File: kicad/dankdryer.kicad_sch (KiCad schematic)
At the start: 25 parts, among them J11 testpin, J13 barreljack, J8 motor, J9 Conn_01x04, SW2 bootmode, U1 TPS62132, U6 ESP32-C6-MINI-1U

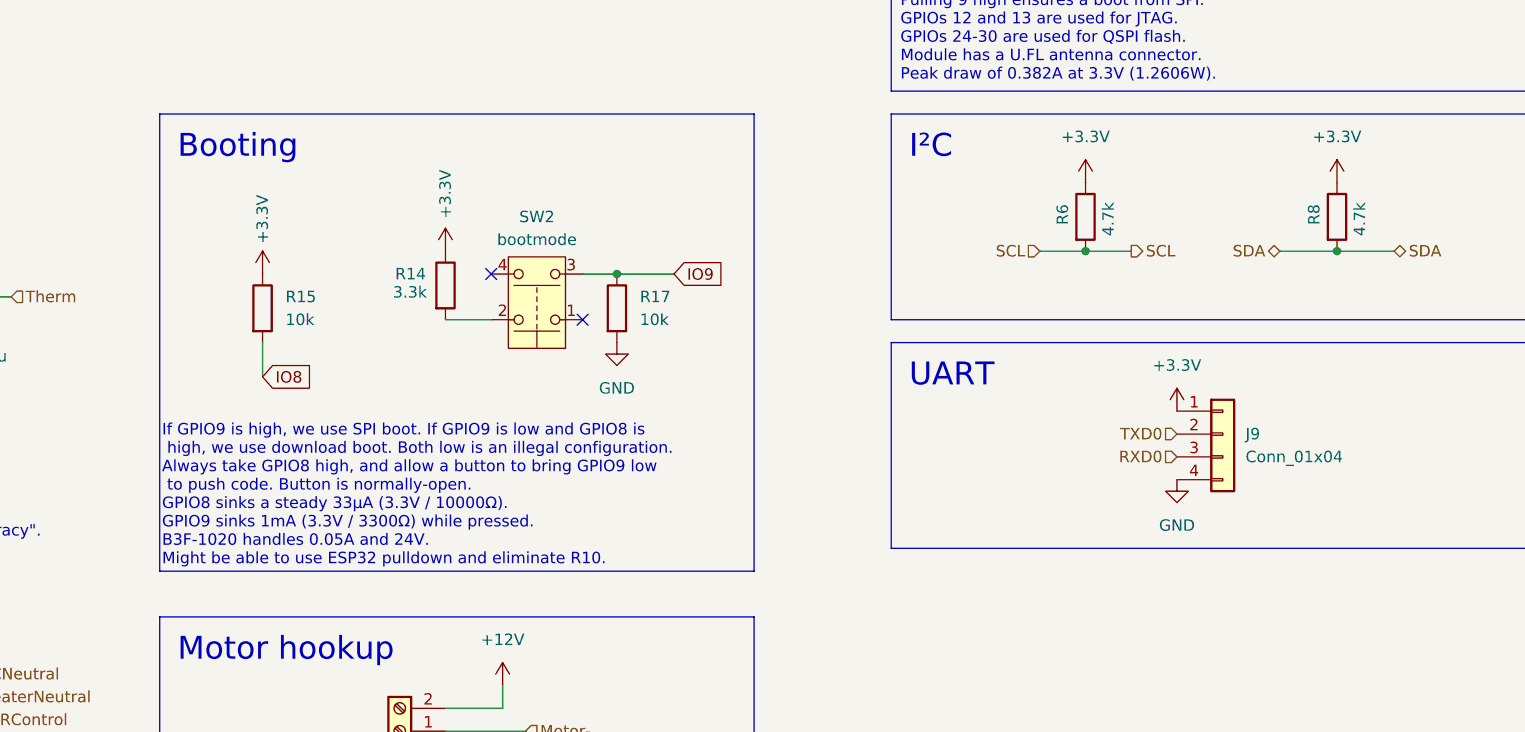
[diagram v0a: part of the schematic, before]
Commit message: invert logic for gpio9, erp
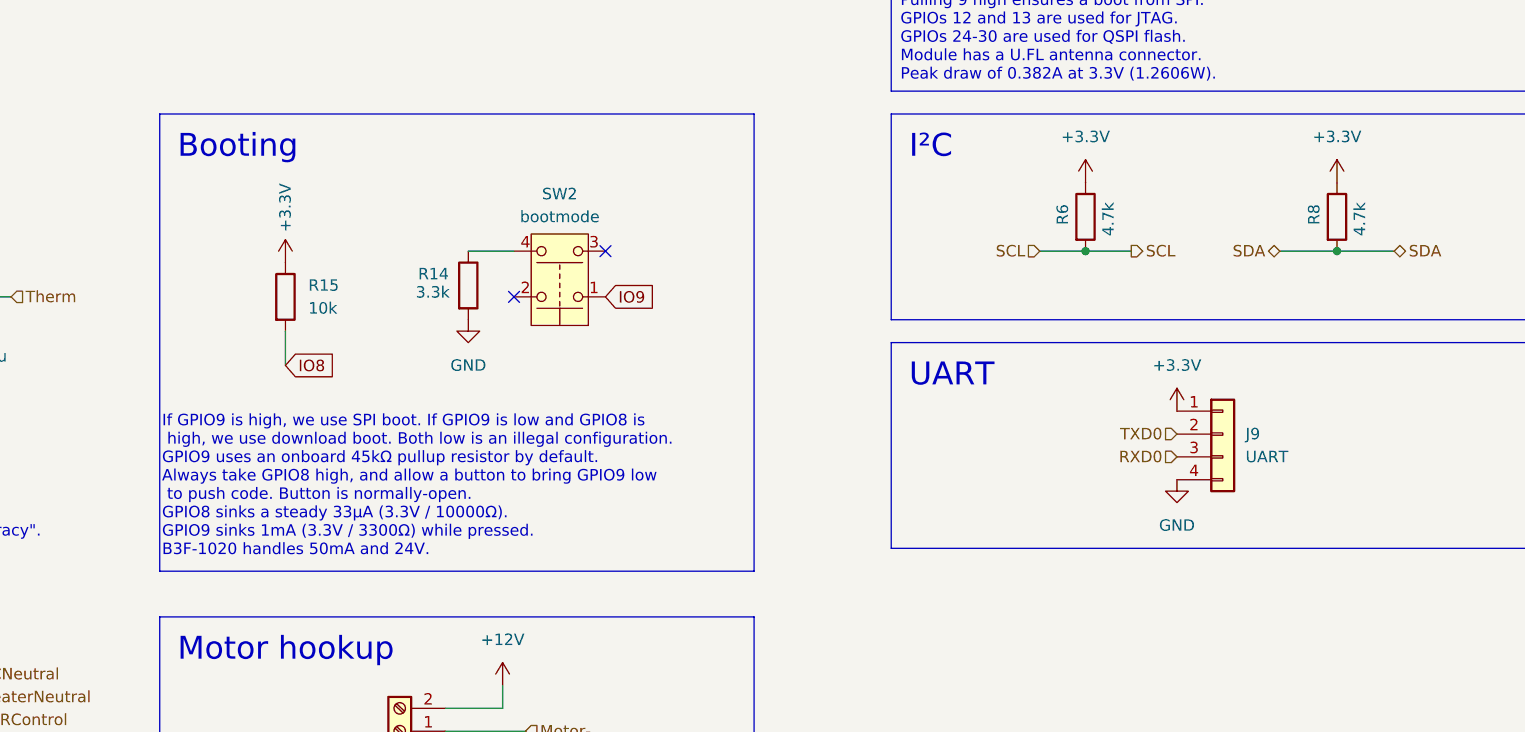
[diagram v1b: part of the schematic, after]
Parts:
- removed R17: 10k, Resistor_SMD:R_1206_3216Metric_Pad1.30x1.75mm_HandSolder, symbol Device:R
- J9: value Conn_01x04 -> UART
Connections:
- net +3.3V: no longer R14.1
- net GND: now also R14.2
- net IO9: now also SW2.1; no longer SW2.3
- net at SW2.2: no longer R14.2
- net at SW2.4: now also R14.1
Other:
- note added: "If GPIO9 is high, we use SPI boot. If GPIO9 is low and GPIO8 is high, we use download boot. Both low is an illegal configuration. GPIO9 uses an onboard 45kΩ pullup resistor by default. Always take GPIO8 high, and allow a button to bring GPIO9 low to push code. Button is normally-open. GPIO8 sinks a steady 33μA (3.3V / 10000Ω). GPIO9 sinks 1mA (3.3V / 3300Ω) while pressed. B3F-1020 handles 50mA an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"
- note removed: "If GPIO9 is high, we use SPI boot. If GPIO9 is low and GPIO8 is high, we use download boot. Both low is an illegal configuration. Always take GPIO8 high, and allow a button to bring GPIO9 low to push code. Button is normally-open. GPIO8 sinks a steady 33μA (3.3V / 10000Ω). GPIO9 sinks 1mA (3.3V / 3300Ω) while pressed. B3F-1020 handles 0.05A and 24V. Might be able to use ESP32 pulldown and elimina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"
- moved on the sheet: R14, R15, SW2

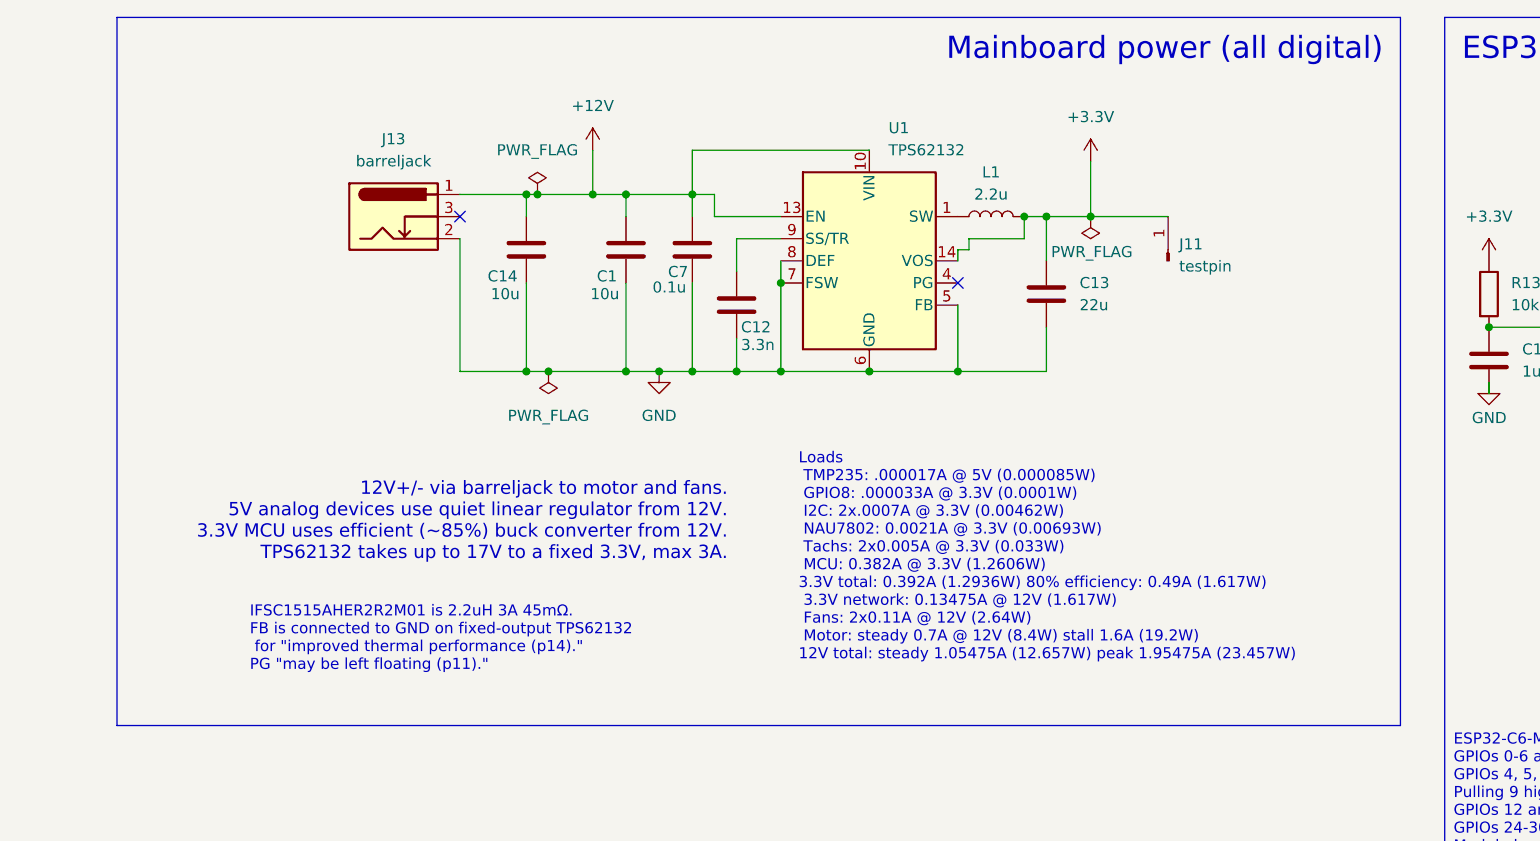
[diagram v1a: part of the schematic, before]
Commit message: switch from AKL_R to regular
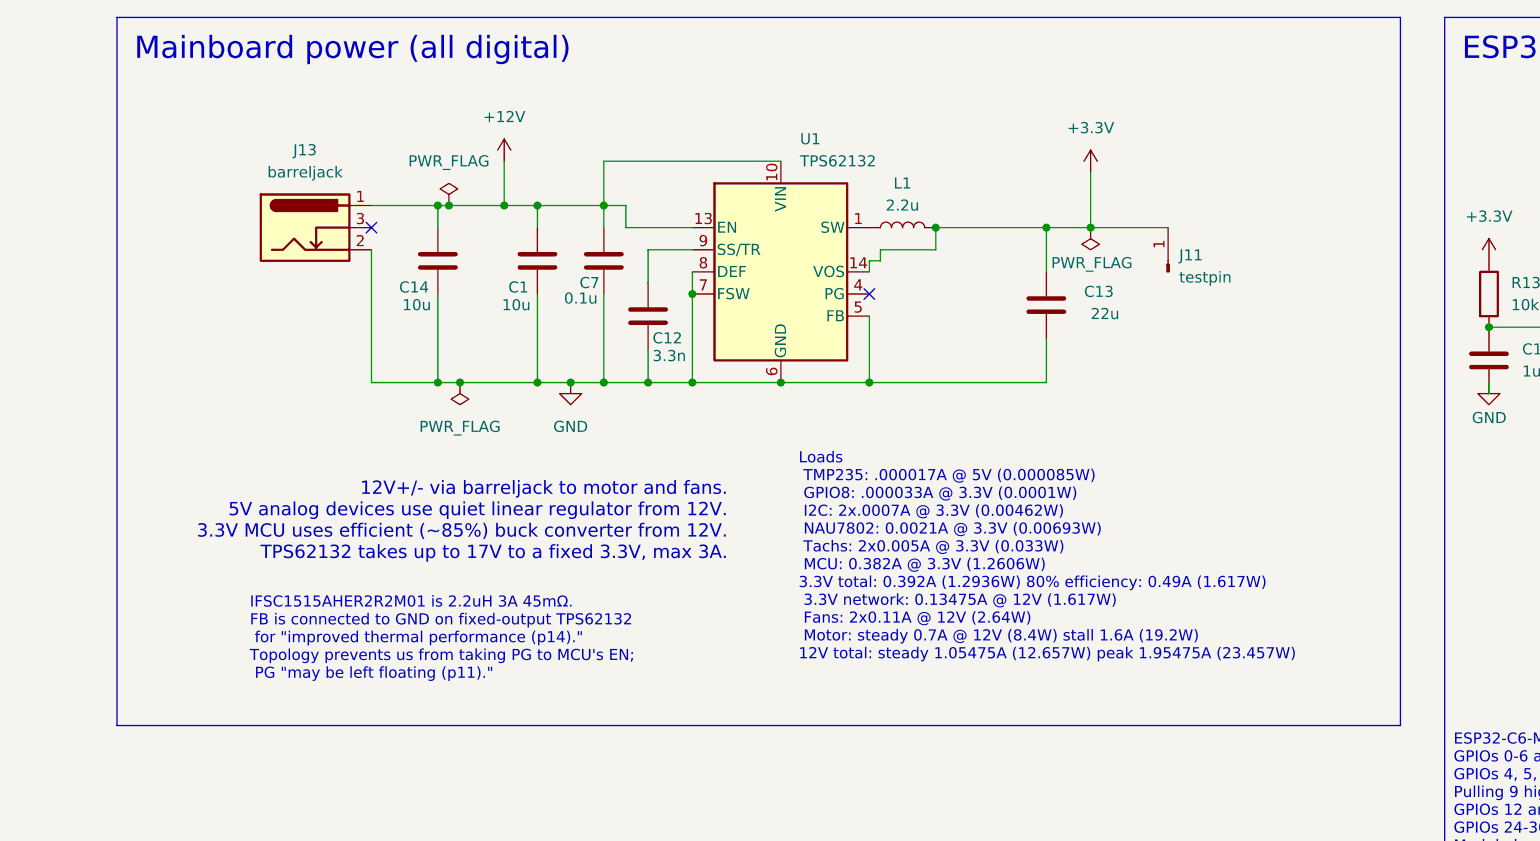
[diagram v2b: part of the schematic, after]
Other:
- note added: "IFSC1515AHER2R2M01 is 2.2uH 3A 45mΩ. FB is connected to GND on fixed-output TPS62132 for "improved thermal performance (p14)." Topology prevents us from taking PG to MCU's EN; PG "may be left floating (p11).""
- note removed: "IFSC1515AHER2R2M01 is 2.2uH 3A 45mΩ. FB is connected to GND on fixed-output TPS62132 for "improved thermal performance (p14)." PG "may be left floating (p11).""
- moved on the sheet: C1, C12, C13, C14, C7, J11, J13, L1, U1

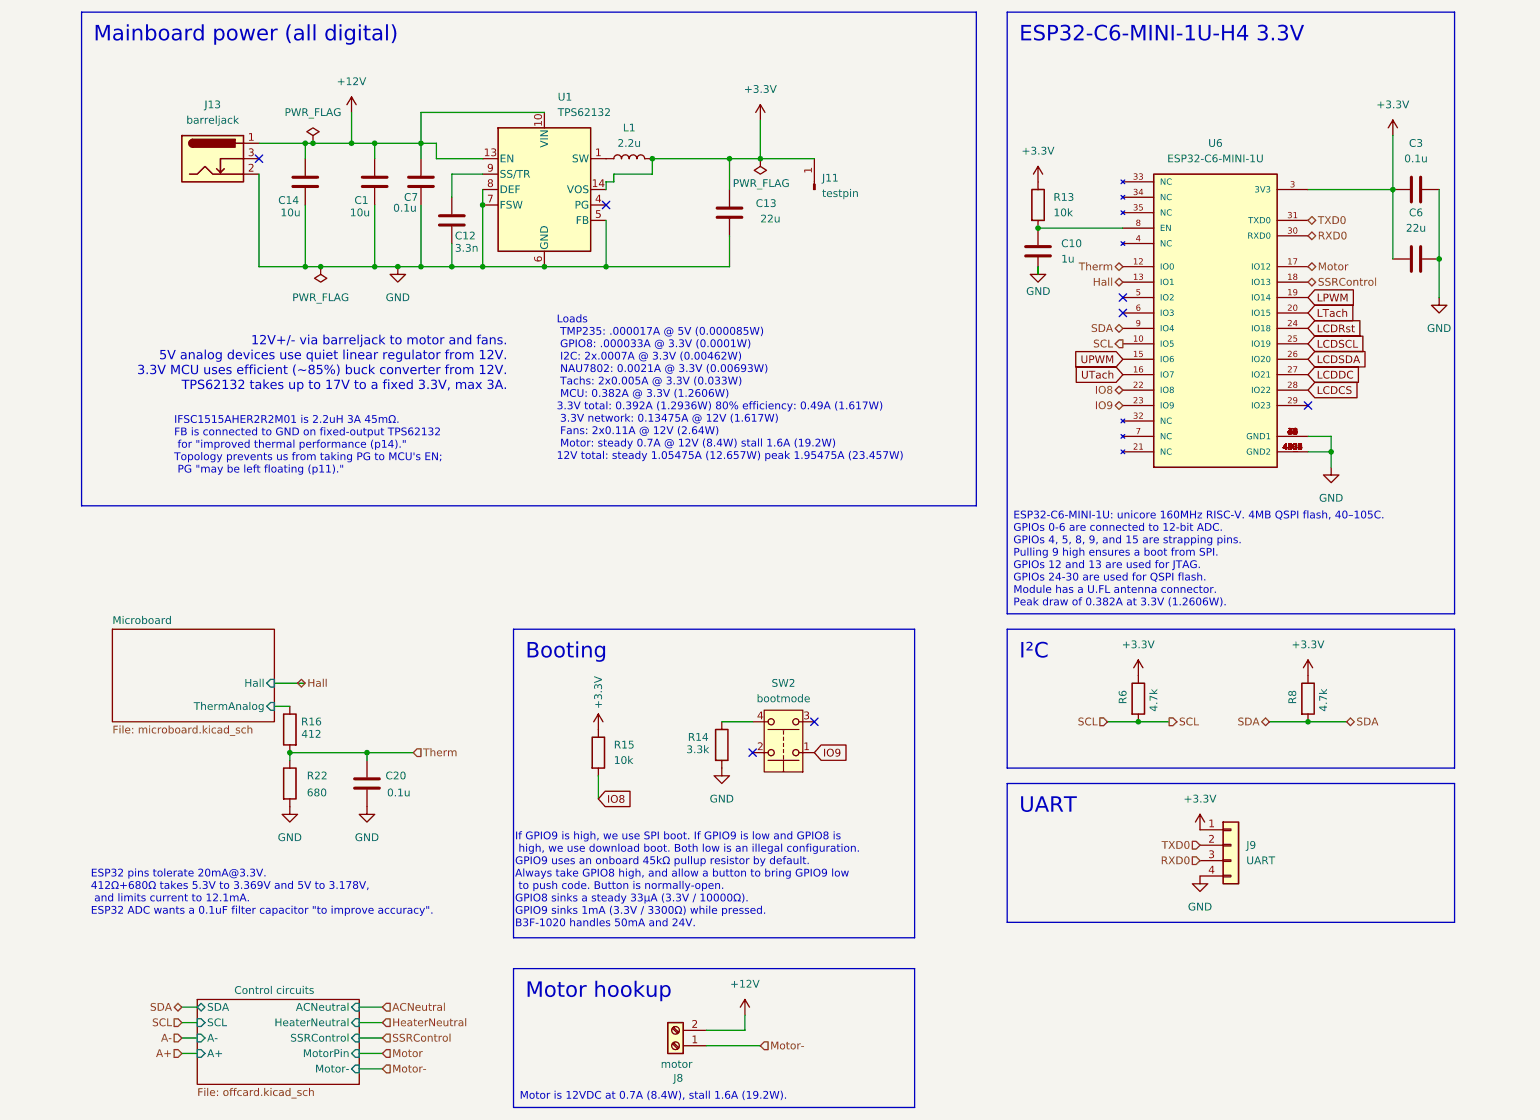
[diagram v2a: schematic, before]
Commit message: upgrade to kicad9
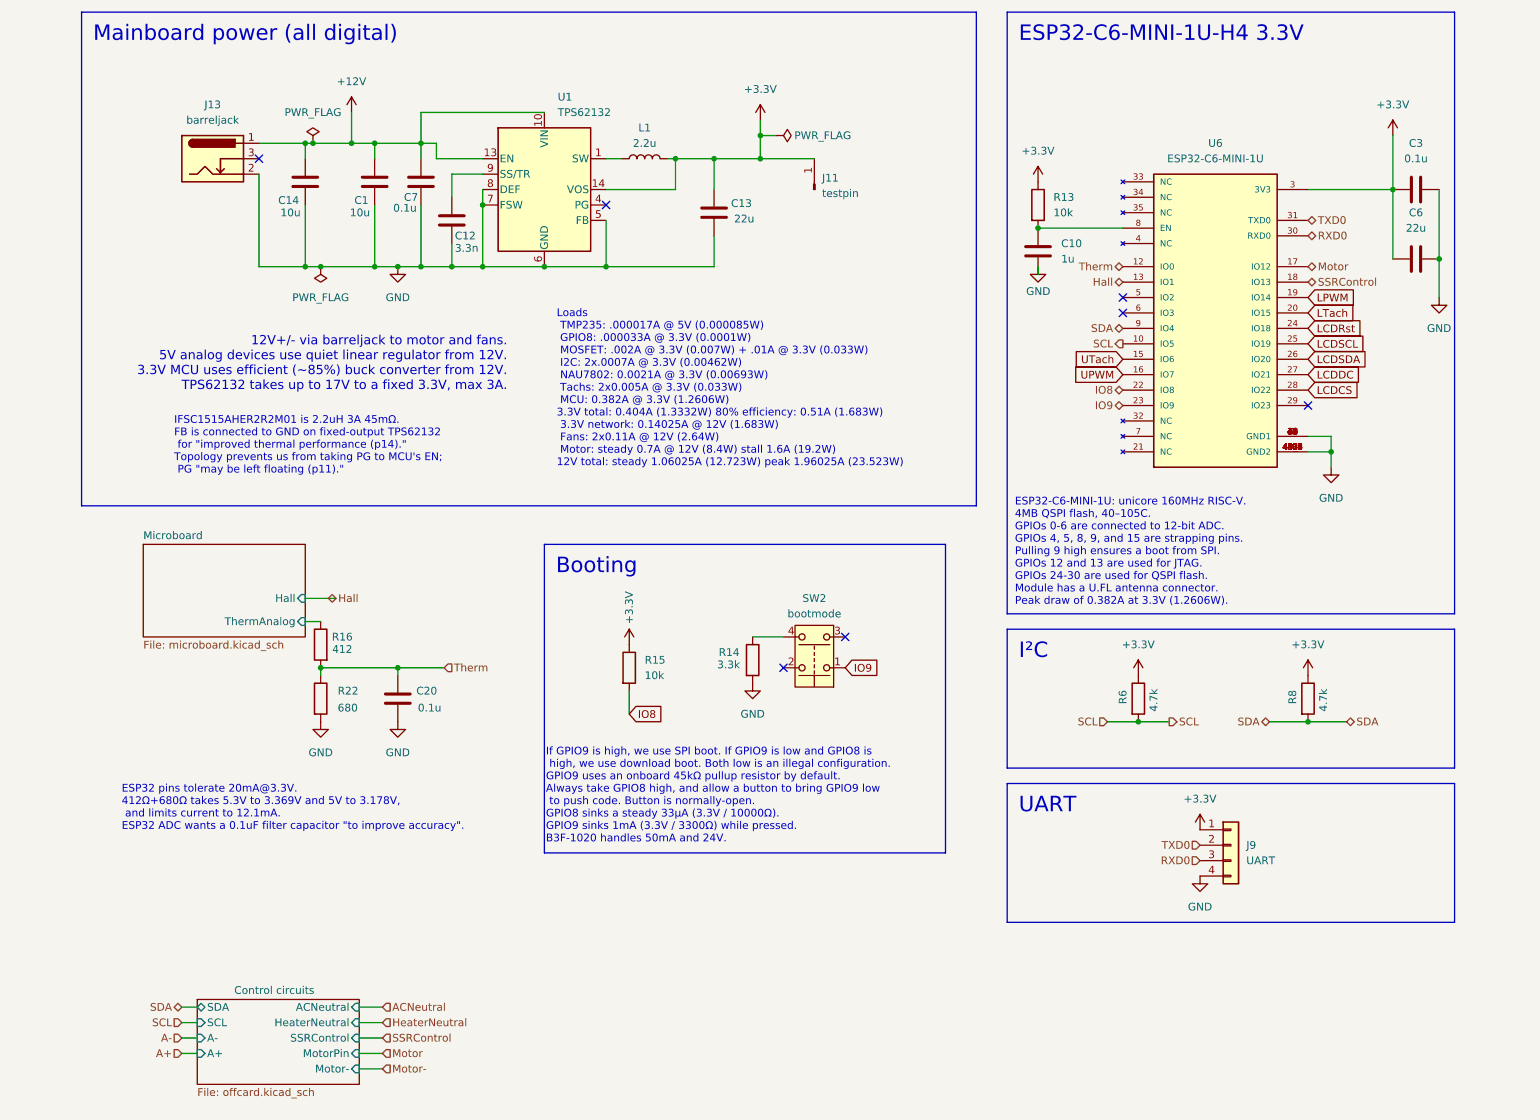
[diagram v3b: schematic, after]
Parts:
- removed J8: motor, dank:TerminalBlock_bornier-2_P5.08mm, symbol Connector:Screw_Terminal_01x02
- R14: footprint PCM_Resistor_SMD_AKL:R_1206_3216Metric_Pad1.30x1.75mm_HandSolder -> Resistor_SMD:R_1206_3216Metric_Pad1.30x1.75mm_HandSolder
- U6: footprint dank:XCVR_ESP32-C6-MINI-1U-H4 -> dank:ESP32-C6-MINI-1U-H4
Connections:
- net UPWM: now also U6.16 (IO7); no longer U6.15 (IO6)
- net UTach: now also U6.15 (IO6); no longer U6.16 (IO7)
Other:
- note added: "Loads TMP235: .000017A @ 5V (0.000085W) GPIO8: .000033A @ 3.3V (0.0001W) MOSFET: .002A @ 3.3V (0.007W) + .01A @ 3.3V (0.033W) I2C: 2x.0007A @ 3.3V (0.00462W) NAU7802: 0.0021A @ 3.3V (0.00693W) Tachs: 2x0.005A @ 3.3V (0.033W) MCU: 0.382A @ 3.3V (1.2606W) 3.3V total: 0.404A (1.3332W) 80% efficiency: 0.51A (1.683W) 3.3V network: 0.14025A @ 12V (1.683W) Fans: 2x0.11A @ 12V (2.64W) Motor: steady 0.7A 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"
- note removed: "Loads TMP235: .000017A @ 5V (0.000085W) GPIO8: .000033A @ 3.3V (0.0001W) I2C: 2x.0007A @ 3.3V (0.00462W) NAU7802: 0.0021A @ 3.3V (0.00693W) Tachs: 2x0.005A @ 3.3V (0.033W) MCU: 0.382A @ 3.3V (1.2606W) 3.3V total: 0.392A (1.2936W) 80% efficiency: 0.49A (1.617W) 3.3V network: 0.13475A @ 12V (1.617W) Fans: 2x0.11A @ 12V (2.64W) Motor: steady 0.7A @ 12V (8.4W) stall 1.6A (19.2W) 12V total: steady 1.0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"
- note removed: "Motor is 12VDC at 0.7A (8.4W), stall 1.6A (19.2W)."
- moved on the sheet: C13, C20, L1, R14, R15, R16, R22, SW2
